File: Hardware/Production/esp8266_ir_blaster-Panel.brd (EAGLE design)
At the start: 97.3 x 103.8 mm, 384 parts, among them Q1 600mA/40V, Q2 600mA/40V, Q3 600mA/40V, Q4 600mA/40V, Q5 600mA/40V, Q6 600mA/40V, Q7 600mA/40V, Q8 600mA/40V, Q9 600mA/40V, U1 ESP-12S, U10 38kHz, U11 ESP-12S, U12 38kHz, U13 ESP-12S, U14 38kHz, U15 ESP-12S, U16 38kHz, U17 ESP-12S, U18 38kHz, U2 38kHz, U3 ESP-12S, U4 38kHz, U5 ESP-12S, U6 38kHz, U7 ESP-12S, U8 38kHz, U9 ESP-12S

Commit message: Revising LED color. Adding production panel.
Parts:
- D11, D14, D17, D2, D20, D23, D26, D5, D8: value BLUE -> GREEN
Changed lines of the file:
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@@
 <?xml version="1.0" encoding="utf-8"?>
 <!DOCTYPE eagle SYSTEM "eagle.dtd">
-<eagle version="9.0.1">
+<eagle version="9.1.1">
 <drawing>
 <settings>
@@
 <param name="checkStop" value="0"/>
 <param name="checkValues" value="0"/>
+<param name="checkNames" value="1"/>
+<param name="checkWireStubs" value="1"/>
+<param name="checkPolygonWidth" value="0"/>
 <param name="useDiameter" value="13"/>
 <param name="maxErrors" value="50"/>
@@
 <attribute name="PROD_ID" value="RES-07856" x="14.351" y="15.875" size="1.778" layer="27" font="vector" ratio="15" rot="R90" display="off"/>
 </element>
-<element name="D2" library="SparkFun-LED" package="LED-0603" value="BLUE" x="12.7" y="15.875" rot="R90">
-<attribute name="PROD_ID" value="DIO-08575" x="12.7" y="15.875" size="1.778" layer="27" font="vector" ratio="15" rot="R90" display="off"/>
+<element name="D2" library="SparkFun-LED" package="LED-0603" value="GREEN" x="12.7" y="15.875" rot="R90">
+<attribute name="PROD_ID" value="DIO-00821" x="12.7" y="15.875" size="1.778" layer="27" font="vector" ratio="15" rot="R90" display="off"/>
 </element>
 <element name="Q1" library="SparkFun-DiscreteSemi" package="SOT23-3" value="600mA/40V" x="13.97" y="5.08" rot="R90">
@@
 <attribute name="PROD_ID" value="RES-07856" x="40.259" y="15.875" size="1.778" layer="27" font="vector" ratio="15" rot="R90" display="off"/>
 </element>
-<element name="D5" library="SparkFun-LED" package="LED-0603" value="BLUE" x="38.608" y="15.875" rot="R90">
-<attribute name="PROD_ID" value="DIO-08575" x="38.608" y="15.875" size="1.778" layer="27" font="vector" ratio="15" rot="R90" display="off"/>
+<element name="D5" library="SparkFun-LED" package="LED-0603" value="GREEN" x="38.608" y="15.875" rot="R90">
+<attribute name="PROD_ID" value="DIO-00821" x="38.608" y="15.875" size="1.778" layer="27" font="vector" ratio="15" rot="R90" display="off"/>
 </element>
 <element name="Q2" library="SparkFun-DiscreteSemi" package="SOT23-3" value="600mA/40V" x="39.878" y="5.08" rot="R90">
@@
 <attribute name="PROD_ID" value="RES-07856" x="66.167" y="15.875" size="1.778" layer="27" font="vector" ratio="15" rot="R90" display="off"/>
 </element>
-<element name="D8" library="SparkFun-LED" package="LED-0603" value="BLUE" x="64.516" y="15.875" rot="R90">
-<attribute name="PROD_ID" value="DIO-08575" x="64.516" y="15.875" size="1.778" layer="27" font="vector" ratio="15" rot="R90" display="off"/>
+<element name="D8" library="SparkFun-LED" package="LED-0603" value="GREEN" x="64.516" y="15.875" rot="R90">
+<attribute name="PROD_ID" value="DIO-00821" x="64.516" y="15.875" size="1.778" layer="27" font="vector" ratio="15" rot="R90" display="off"/>
 </element>
 <element name="Q3" library="SparkFun-DiscreteSemi" package="SOT23-3" value="600mA/40V" x="65.786" y="5.08" rot="R90">
@@
 <attribute name="PROD_ID" value="RES-07856" x="14.351" y="43.942" size="1.778" layer="27" font="vector" ratio="15" rot="R90" display="off"/>
 </element>
-<element name="D11" library="SparkFun-LED" package="LED-0603" value="BLUE" x="12.7" y="43.942" rot="R90">
-<attribute name="PROD_ID" value="DIO-08575" x="12.7" y="43.942" size="1.778" layer="27" font="vector" ratio="15" rot="R90" display="off"/>
+<element name="D11" library="SparkFun-LED" package="LED-0603" value="GREEN" x="12.7" y="43.942" rot="R90">
+<attribute name="PROD_ID" value="DIO-00821" x="12.7" y="43.942" size="1.778" layer="27" font="vector" ratio="15" rot="R90" display="off"/>
 </element>
 <element name="Q4" library="SparkFun-DiscreteSemi" package="SOT23-3" value="600mA/40V" x="13.97" y="33.147" rot="R90">
@@
 <attribute name="PROD_ID" value="RES-07856" x="40.259" y="43.942" size="1.778" layer="27" font="vector" ratio="15" rot="R90" display="off"/>
 </element>
-<element name="D14" library="SparkFun-LED" package="LED-0603" value="BLUE" x="38.608" y="43.942" rot="R90">
-<attribute name="PROD_ID" value="DIO-08575" x="38.608" y="43.942" size="1.778" layer="27" font="vector" ratio="15" rot="R90" display="off"/>
+<element name="D14" library="SparkFun-LED" package="LED-0603" value="GREEN" x="38.608" y="43.942" rot="R90">
+<attribute name="PROD_ID" value="DIO-00821" x="38.608" y="43.942" size="1.778" layer="27" font="vector" ratio="15" rot="R90" display="off"/>
 </element>
 <element name="Q5" library="SparkFun-DiscreteSemi" package="SOT23-3" value="600mA/40V" x="39.878" y="33.147" rot="R90">
@@
 <attribute name="PROD_ID" value="RES-07856" x="66.167" y="43.942" size="1.778" layer="27" font="vector" ratio="15" rot="R90" display="off"/>
 </element>
-<element name="D17" library="SparkFun-LED" package="LED-0603" value="BLUE" x="64.516" y="43.942" rot="R90">
-<attribute name="PROD_ID" value="DIO-08575" x="64.516" y="43.942" size="1.778" layer="27" font="vector" ratio="15" rot="R90" display="off"/>
+<element name="D17" library="SparkFun-LED" package="LED-0603" value="GREEN" x="64.516" y="43.942" rot="R90">
+<attribute name="PROD_ID" value="DIO-00821" x="64.516" y="43.942" size="1.778" layer="27" font="vector" ratio="15" rot="R90" display="off"/>
 </element>
 <element name="Q6" library="SparkFun-DiscreteSemi" package="SOT23-3" value="600mA/40V" x="65.786" y="33.147" rot="R90">
@@
 <attribute name="PROD_ID" value="RES-07856" x="14.351" y="72.009" size="1.778" layer="27" font="vector" ratio="15" rot="R90" display="off"/>
 </element>
-<element name="D20" library="SparkFun-LED" package="LED-0603" value="BLUE" x="12.7" y="72.009" rot="R90">
-<attribute name="PROD_ID" value="DIO-08575" x="12.7" y="72.009" size="1.778" layer="27" font="vector" ratio="15" rot="R90" display="off"/>
+<element name="D20" library="SparkFun-LED" package="LED-0603" value="GREEN" x="12.7" y="72.009" rot="R90">
+<attribute name="PROD_ID" value="DIO-00821" x="12.7" y="72.009" size="1.778" layer="27" font="vector" ratio="15" rot="R90" display="off"/>
 </element>
 <element name="Q7" library="SparkFun-DiscreteSemi" package="SOT23-3" value="600mA/40V" x="13.97" y="61.214" rot="R90">
@@
 <attribute name="PROD_ID" value="RES-07856" x="40.259" y="72.009" size="1.778" layer="27" font="vector" ratio="15" rot="R90" display="off"/>
 </element>
-<element name="D23" library="SparkFun-LED" package="LED-0603" value="BLUE" x="38.608" y="72.009" rot="R90">
-<attribute name="PROD_ID" value="DIO-08575" x="38.608" y="72.009" size="1.778" layer="27" font="vector" ratio="15" rot="R90" display="off"/>
+<element name="D23" library="SparkFun-LED" package="LED-0603" value="GREEN" x="38.608" y="72.009" rot="R90">
+<attribute name="PROD_ID" value="DIO-00821" x="38.608" y="72.009" size="1.778" layer="27" font="vector" ratio="15" rot="R90" display="off"/>
 </element>
 <element name="Q8" library="SparkFun-DiscreteSemi" package="SOT23-3" value="600mA/40V" x="39.878" y="61.214" rot="R90">
@@
 <attribute name="PROD_ID" value="RES-07856" x="66.167" y="72.009" size="1.778" layer="27" font="vector" ratio="15" rot="R90" display="off"/>
 </element>
-<element name="D26" library="SparkFun-LED" package="LED-0603" value="BLUE" x="64.516" y="72.009" rot="R90">
-<attribute name="PROD_ID" value="DIO-08575" x="64.516" y="72.009" size="1.778" layer="27" font="vector" ratio="15" rot="R90" display="off"/>
+<element name="D26" library="SparkFun-LED" package="LED-0603" value="GREEN" x="64.516" y="72.009" rot="R90">
+<attribute name="PROD_ID" value="DIO-00821" x="64.516" y="72.009" size="1.778" layer="27" font="vector" ratio="15" rot="R90" display="off"/>
 </element>
 <element name="Q9" library="SparkFun-DiscreteSemi" package="SOT23-3" value="600mA/40V" x="65.786" y="61.214" rot="R90">
@@
 </signal>
 </signals>
+<mfgpreviewcolors>
+<mfgpreviewcolor name="soldermaskcolor" color="0xC8008000"/>
+<mfgpreviewcolor name="silkscreencolor" color="0xFFFEFEFE"/>
+<mfgpreviewcolor name="backgroundcolor" color="0xFF282828"/>
+<mfgpreviewcolor name="coppercolor" color="0xFFFFBF00"/>
+<mfgpreviewcolor name="substratecolor" color="0xFF786E46"/>
+</mfgpreviewcolors>
 </board>
 </drawing>

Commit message: x02 hardware commit
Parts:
- added C10, C11, C13, C14, C15, C17, C18, C19, C21, C22, C23, C25, C26, C27, C29, C30, C31, C33, C34, C35: 1.0uF, SparkFun-Capacitors:0603
- added C12, C16, C20, C24, C28, C32, C36: 2.2uF, SparkFun-Capacitors:0603
- added H1, H10, H11, H12, H13, H14, H15, H16, H17, H18, H2, H3, H4, H5, H6, H7, H8, H9: STAND-OFF, SparkFun-Hardware:STAND-OFF
- added R64, R68, R70, R72: 1k, SparkFun-Resistors:0603
- added R65, R66, R67, R71: 10k, SparkFun-Resistors:0603
- added R69: 20, SparkFun-Resistors:0603
- added U$154, U$174: (no value), buzzard_labels:VIN6
- added U$155, U$168, U$175: (no value), buzzard_labels:GND5
- added U$156, U$176: (no value), buzzard_labels:512
- added U$157, U$167, U$177: (no value), buzzard_labels:3#3V4
- added U$158, U$178: (no value), buzzard_labels:SLP14
- added U$159, U$161, U$179: (no value), buzzard_labels:WIFI_IR_BLASTER11
- added U$160, U$180: (no value), buzzard_labels-02:UART0
- added U$162: (no value), buzzard_labels:013
- added U$163: (no value), buzzard_labels:RST14
- added U$164: (no value), buzzard_labels:DTR1
- added U$165: (no value), buzzard_labels:TX2
- added U$166: (no value), buzzard_labels:RX3
- added U$169: (no value), buzzard_labels:511
- added U$170: (no value), buzzard_labels:ADC10
- added U$171: (no value), buzzard_labels:129
- added U$172: (no value), buzzard_labels:148
- added U$173: (no value), buzzard_labels:27
- added U19, U22, U25: ESP-12S, esp8266_ir_blaster:ESP-12S
- added U20, U23, U26: 38kHz, esp8266_ir_blaster:TSOP382
- added U21, U24, U27: 3.3V, SparkFun-IC-Power:SOT23-5
- C4, C8: value 1.0uF -> 2.2uF
- J1, J11, J13, J15, J17, J9: device SparkFun-Connectors:1X06 -> SparkFun-Connectors:1X06_NO_SILK
- J10, J12, J14, J16, J18, J8: device SparkFun-Connectors:1X07 -> SparkFun-Connectors:1X08_NO_SILK
- J2, J4, J6: device SparkFun-Connectors:1X06 -> SparkFun-Connectors:1X08_NO_SILK
- J3, J5, J7: device SparkFun-Connectors:1X07 -> SparkFun-Connectors:1X06_NO_SILK
- R11, R18, R25, R27, R34, R39, R41, R55: value 1k -> 10k
- R12, R40, R54: value 68 -> 1k
- R13, R53: value 1k -> 20
- R14, R16, R22, R24, R28, R3, R30, R36, R38, R44, R52, R56: value 10k -> 1k
- R19, R26, R33, R47: value 68 -> 10k
- R21, R29, R37, R45: value 10k -> 20
- R6, R61: value 68 -> 20
- U$1: device buzzard_labels:GND11 -> buzzard_labels:512
- U$10: device buzzard_labels:RX3 -> buzzard_labels:129
- U$100: device buzzard_labels:RST14 -> buzzard_labels-02:UART0
- U$101, U$99: device buzzard_labels:013 -> buzzard_labels:WIFI_IR_BLASTER11
- U$102: device buzzard_labels:SLEEP15 -> buzzard_labels:013
- U$103: device buzzard_labels:GND11 -> buzzard_labels:RST14
- U$104: device buzzard_labels:3#3V12 -> buzzard_labels:DTR1
- U$105: device buzzard_labels:210 -> buzzard_labels:TX2
- U$106: device buzzard_labels:149 -> buzzard_labels:RX3
- U$107: device buzzard_labels:127 -> buzzard_labels:3#3V4
- U$108: device buzzard_labels:ADC6 -> buzzard_labels:GND5
- U$109: device buzzard_labels:58 -> buzzard_labels:511
- U$11: device buzzard_labels:TX4 -> buzzard_labels:148
- U$110: device buzzard_labels:GND1 -> buzzard_labels:ADC10
- U$111: device buzzard_labels:3#3V2 -> buzzard_labels:129
- U$112: device buzzard_labels:RX3 -> buzzard_labels:148
- U$113: device buzzard_labels:TX4 -> buzzard_labels:27
- U$114: device buzzard_labels:DTR5 -> buzzard_labels:VIN6
- U$115: device buzzard_labels:WIFI_IR_BLASTER11 -> buzzard_labels:GND5
- U$116: device buzzard_labels:013 -> buzzard_labels:512
- U$117: device buzzard_labels:RST14 -> buzzard_labels:3#3V4
- U$118: device buzzard_labels:013 -> buzzard_labels:SLP14
- U$119: device buzzard_labels:SLEEP15 -> buzzard_labels:WIFI_IR_BLASTER11
- U$12: device buzzard_labels:DTR5 -> buzzard_labels:27
- U$120: device buzzard_labels:GND11 -> buzzard_labels-02:UART0
- U$121: device buzzard_labels:3#3V12 -> buzzard_labels:WIFI_IR_BLASTER11
- U$122: device buzzard_labels:210 -> buzzard_labels:013
- U$123: device buzzard_labels:149 -> buzzard_labels:RST14
- U$124: device buzzard_labels:127 -> buzzard_labels:DTR1
- U$125: device buzzard_labels:ADC6 -> buzzard_labels:TX2
- U$126: device buzzard_labels:58 -> buzzard_labels:RX3
- U$127: device buzzard_labels:GND1 -> buzzard_labels:3#3V4
- U$128: device buzzard_labels:3#3V2 -> buzzard_labels:GND5
- U$129: device buzzard_labels:RX3 -> buzzard_labels:511
- U$130: device buzzard_labels:TX4 -> buzzard_labels:ADC10
- U$131: device buzzard_labels:DTR5 -> buzzard_labels:129
- U$132: device buzzard_labels:WIFI_IR_BLASTER11 -> buzzard_labels:148
- U$133, U$33: device buzzard_labels:013 -> buzzard_labels:27
- U$134: device buzzard_labels:RST14 -> buzzard_labels:VIN6
- U$135, U$48: device buzzard_labels:013 -> buzzard_labels:GND5
- U$136: device buzzard_labels:SLEEP15 -> buzzard_labels:512
- U$137: device buzzard_labels:GND11 -> buzzard_labels:3#3V4
- U$138: device buzzard_labels:3#3V12 -> buzzard_labels:SLP14
- U$139: device buzzard_labels:210 -> buzzard_labels:WIFI_IR_BLASTER11
- U$140: device buzzard_labels:149 -> buzzard_labels-02:UART0
- U$141, U$39: device buzzard_labels:127 -> buzzard_labels:WIFI_IR_BLASTER11
- U$142: device buzzard_labels:ADC6 -> buzzard_labels:013
- U$143: device buzzard_labels:58 -> buzzard_labels:RST14
- U$144: device buzzard_labels:GND1 -> buzzard_labels:DTR1
- U$145: device buzzard_labels:3#3V2 -> buzzard_labels:TX2
- U$147: device buzzard_labels:TX4 -> buzzard_labels:3#3V4
- U$148: device buzzard_labels:DTR5 -> buzzard_labels:GND5
- U$149: device buzzard_labels:WIFI_IR_BLASTER11 -> buzzard_labels:511
- U$150, U$50: device buzzard_labels:013 -> buzzard_labels:ADC10
- U$151: device buzzard_labels:RST14 -> buzzard_labels:129
- U$152: device buzzard_labels:013 -> buzzard_labels:148
- U$153: device buzzard_labels:SLEEP15 -> buzzard_labels:27
- U$17: device buzzard_labels:SLEEP15 -> buzzard_labels:RST14
- U$18: device buzzard_labels:GND11 -> buzzard_labels:DTR1
- U$19: device buzzard_labels:3#3V12 -> buzzard_labels:TX2
- U$2, U$87: device buzzard_labels:3#3V12 -> buzzard_labels:3#3V4
- U$20: device buzzard_labels:210 -> buzzard_labels:RX3
- U$21: device buzzard_labels:149 -> buzzard_labels:3#3V4
- U$22: device buzzard_labels:127 -> buzzard_labels:GND5
- U$23, U$74: device buzzard_labels:ADC6 -> buzzard_labels:VIN6
- U$24, U$75: device buzzard_labels:58 -> buzzard_labels:GND5
- U$25: device buzzard_labels:GND1 -> buzzard_labels:TX2
- U$26: device buzzard_labels:3#3V2 -> buzzard_labels:RX3
- U$27: device buzzard_labels:RX3 -> buzzard_labels:3#3V4
- U$28: device buzzard_labels:TX4 -> buzzard_labels:GND5
- U$29: device buzzard_labels:DTR5 -> buzzard_labels:511
- U$3: device buzzard_labels:210 -> buzzard_labels:SLP14
- U$30: device buzzard_labels:WIFI_IR_BLASTER11 -> buzzard_labels:ADC10
- U$31: device buzzard_labels:013 -> buzzard_labels:129
- U$32: device buzzard_labels:RST14 -> buzzard_labels:148
- U$34: device buzzard_labels:SLEEP15 -> buzzard_labels:VIN6
- U$35: device buzzard_labels:GND11 -> buzzard_labels:GND5
- U$36: device buzzard_labels:3#3V12 -> buzzard_labels:512
- U$37: device buzzard_labels:210 -> buzzard_labels:3#3V4
- U$38: device buzzard_labels:149 -> buzzard_labels:SLP14
- U$4: device buzzard_labels:149 -> buzzard_labels:WIFI_IR_BLASTER11
- U$40: device buzzard_labels:ADC6 -> buzzard_labels-02:UART0
- U$41, U$7: device buzzard_labels:58 -> buzzard_labels:WIFI_IR_BLASTER11
- U$42: device buzzard_labels:GND1 -> buzzard_labels:013
- U$43: device buzzard_labels:3#3V2 -> buzzard_labels:RST14
- U$44: device buzzard_labels:RX3 -> buzzard_labels:DTR1
- U$45: device buzzard_labels:TX4 -> buzzard_labels:TX2
- U$46: device buzzard_labels:DTR5 -> buzzard_labels:RX3
- U$47: device buzzard_labels:WIFI_IR_BLASTER11 -> buzzard_labels:3#3V4
- U$49: device buzzard_labels:RST14 -> buzzard_labels:511
- U$5: device buzzard_labels:127 -> buzzard_labels-02:UART0
- U$51: device buzzard_labels:SLEEP15 -> buzzard_labels:129
- U$52: device buzzard_labels:GND11 -> buzzard_labels:148
- U$53: device buzzard_labels:3#3V12 -> buzzard_labels:27
- U$54: device buzzard_labels:210 -> buzzard_labels:VIN6
- U$55: device buzzard_labels:149 -> buzzard_labels:GND5
- U$56: device buzzard_labels:127 -> buzzard_labels:512
- U$57: device buzzard_labels:ADC6 -> buzzard_labels:3#3V4
- U$58: device buzzard_labels:58 -> buzzard_labels:SLP14
- U$59: device buzzard_labels:GND1 -> buzzard_labels:WIFI_IR_BLASTER11
- U$6: device buzzard_labels:ADC6 -> buzzard_labels:DTR1
- U$60: device buzzard_labels:3#3V2 -> buzzard_labels-02:UART0
- U$61: device buzzard_labels:RX3 -> buzzard_labels:WIFI_IR_BLASTER11
- U$62: device buzzard_labels:TX4 -> buzzard_labels:013
- U$63: device buzzard_labels:DTR5 -> buzzard_labels:RST14
- U$64: device buzzard_labels:WIFI_IR_BLASTER11 -> buzzard_labels:DTR1
- U$65: device buzzard_labels:013 -> buzzard_labels:TX2
- U$66: device buzzard_labels:RST14 -> buzzard_labels:RX3
- U$67: device buzzard_labels:013 -> buzzard_labels:3#3V4
- U$68: device buzzard_labels:SLEEP15 -> buzzard_labels:GND5
- U$69: device buzzard_labels:GND11 -> buzzard_labels:511
- U$70: device buzzard_labels:3#3V12 -> buzzard_labels:ADC10
- U$71: device buzzard_labels:210 -> buzzard_labels:129
- U$72: device buzzard_labels:149 -> buzzard_labels:148
- U$73: device buzzard_labels:127 -> buzzard_labels:27
- U$76: device buzzard_labels:GND1 -> buzzard_labels:512
- U$77: device buzzard_labels:3#3V2 -> buzzard_labels:3#3V4
- U$78: device buzzard_labels:RX3 -> buzzard_labels:SLP14
- U$79: device buzzard_labels:TX4 -> buzzard_labels:WIFI_IR_BLASTER11
- U$8: device buzzard_labels:GND1 -> buzzard_labels:511
- U$80: device buzzard_labels:DTR5 -> buzzard_labels-02:UART0
- U$84: device buzzard_labels:013 -> buzzard_labels:DTR1
- U$85: device buzzard_labels:SLEEP15 -> buzzard_labels:TX2
- U$86: device buzzard_labels:GND11 -> buzzard_labels:RX3
- U$88: device buzzard_labels:210 -> buzzard_labels:GND5
- U$89: device buzzard_labels:149 -> buzzard_labels:511
- U$9: device buzzard_labels:3#3V2 -> buzzard_labels:ADC10
- U$90: device buzzard_labels:127 -> buzzard_labels:ADC10
- U$91: device buzzard_labels:ADC6 -> buzzard_labels:129
- U$92: device buzzard_labels:58 -> buzzard_labels:148
- U$93: device buzzard_labels:GND1 -> buzzard_labels:27
- U$94: device buzzard_labels:3#3V2 -> buzzard_labels:VIN6
- U$95: device buzzard_labels:RX3 -> buzzard_labels:GND5
- U$96: device buzzard_labels:TX4 -> buzzard_labels:512
- U$97: device buzzard_labels:DTR5 -> buzzard_labels:3#3V4
- U$98: device buzzard_labels:WIFI_IR_BLASTER11 -> buzzard_labels:SLP14
- U10, U16, U4: value 38kHz -> ESP-12S; device esp8266_ir_blaster:TSOP382 -> esp8266_ir_blaster:ESP-12S
- U11, U17, U5: value ESP-12S -> 38kHz; device esp8266_ir_blaster:ESP-12S -> esp8266_ir_blaster:TSOP382
- U12, U18, U6: value 38kHz -> 3.3V; device esp8266_ir_blaster:TSOP382 -> SparkFun-IC-Power:SOT23-5
- U15, U3, U9: value ESP-12S -> 3.3V; device esp8266_ir_blaster:ESP-12S -> SparkFun-IC-Power:SOT23-5
- moved J6 82.8 mm to (75.9, 6.35), turned to 90 degrees
- moved U$115 77.2 mm to (70.9, 39.5)
- moved U$59 76.1 mm to (73.4, 2.46), flipped to the bottom
- moved U$114 74.7 mm to (71.2, 42.0)
- moved U$140 74.4 mm to (1.27, 87.1), flipped to the bottom, turned to 90 degrees
- moved U$113 73.7 mm to (73.0, 47.1)
- moved U$112 71.4 mm to (72.4, 52.2)
- moved U$111 71.1 mm to (72.1, 49.7)
- moved U$117 68.7 mm to (70.6, 44.6)
- moved U$110 68.6 mm to (70.7, 54.7)
- moved U$119 67.9 mm to (73.4, 35.6), flipped to the bottom
- moved U$118 66.7 mm to (77.0, 61.3), flipped to the bottom
- moved R44 66.1 mm to (69.0, 47.1), turned to 0 degrees
- moved R22 65.9 mm to (66.7, 11.4), turned to 90 degrees
- moved C7 64.1 mm to (38.7, 11.4)
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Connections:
- removed net N$13 (its old number): D11.C, R25.2
- removed net N$17 (its old number): D14.C, R32.2
- removed net N$2 (its old number): D2.C, R5.2
- removed net N$21 (its old number): D17.C, R39.2
- removed net N$25 (its old number): D20.C, R46.2
- removed net N$29 (its old number): D23.C, R53.2
- removed net N$33 (its old number): D26.C, R60.2
- removed net N$9 (its old number): D8.C, R18.2
- new net N$10: D7.A, R21.1
- new net N$14: D10.A, R29.1
- new net N$18: D13.A, R37.1
- new net N$22: D16.A, R45.1
- new net N$26: D19.A, R53.1
- new net N$3: D4.A, R13.1
- new net N$30: D22.A, R61.1
- new net N$34: D25.A, R69.1
- new net VIN: C3.1, J2.2, U3.1, U3.3
- new net VIN1: C7.1, J4.2, U6.1, U6.3
- new net VIN2: C11.1, J6.2, U9.1, U9.3
- new net VIN3: C15.1, J8.2, U12.1, U12.3
- new net VIN4: C19.1, J10.2, U15.1, U15.3
- new net VIN5: C23.1, J12.2, U18.1, U18.3
- new net VIN6: C27.1, J14.2, U21.1, U21.3
- new net VIN7: C31.1, J16.2, U24.1, U24.3
- new net VIN8: C35.1, J18.2, U27.1, U27.3
- net 3.3V: now also C4.1, J2.3, R5.2, U3.5; no longer D2.A, J8.2
- net 3.3V1: now also C5.1, C8.1, J3.4, J4.3, R10.1, R13.2, R15.1, R9.2, U4.8, U5.3, U6.5; no longer C2.1, D5.A, J2.4, J3.2, R14.1, R3.2, R9.1, U3.8, U4.3
- net 3.3V2: now also C12.1, C9.1, J5.4, J6.3, R17.2, R18.1, R20.2, R21.2, R23.1, U7.8, U8.3, U9.5; no longer C3.1, D8.A, J4.4, J5.2, R15.2, R16.1, R19.2, R21.1, U5.8, U6.3
- net 3.3V3: now also C13.1, C16.1, J7.4, J8.3, R25.2, R26.1, R28.2, R29.2, R31.1, U10.8, U11.3, U12.5; no longer C4.1, D11.A, J6.4, J7.2, R22.2, R23.1, R26.2, R28.1, U7.8, U8.3
- net 3.3V4: now also C17.1, C20.1, J10.3, R34.1, R36.2, R37.2, R39.1, U13.8, U14.3, U15.5; no longer C5.1, D14.A, J10.2, R29.2, R30.1, R35.1, U10.3, U9.8
- net 3.3V5: now also C21.1, C24.1, J12.3, R41.2, R44.2, R45.2, R47.1, U16.8, U17.3, U18.5; no longer C6.1, D17.A, J12.2, R36.2, R37.1, R40.2, U11.8, U12.3
- net 3.3V6: now also C25.1, C28.1, J14.3, R49.2, R50.1, R52.2, R53.2, R55.1, U19.8, U20.3, U21.5; no longer C7.1, D20.A, J14.2, R43.2, R44.1, R47.2, R49.1, U13.8, U14.3
- net 3.3V7: now also C29.1, C32.1, J16.3, R57.2, R58.1, R60.2, R61.2, R63.1, U22.8, U23.3, U24.5; no longer C8.1, D23.A, J16.2, R50.2, R51.1, R54.2, R56.1, U15.8, U16.3
- net 3.3V8: now also C33.1, C36.1, J18.3, R65.2, R66.1, R68.2, R69.2, R71.1, U25.8, U26.3, U27.5; no longer C9.1, D26.A, J18.2, R57.2, R58.1, R61.2, R63.1, U17.8, U18.3
- net ADC: now also J2.7; no longer J8.6
- net ADC1: now also J4.7, U4.2; no longer J3.6, U3.2
- net ADC2: now also J6.7, U7.2; no longer J5.6, U5.2
- net ADC3: now also J8.7, U10.2; no longer J7.6, U7.2
- net ADC4: now also J10.7, U13.2; no longer J10.6, U9.2
- net ADC5: now also J12.7, U16.2; no longer J12.6, U11.2
- net ADC6: now also J14.7, U19.2; no longer J14.6, U13.2
- net ADC7: now also J16.7, U22.2; no longer J16.6, U15.2
- net ADC8: now also J18.7, U25.2; no longer J18.6, U17.2
- net CHIP_EN1: now also R10.2, U4.3; no longer R9.2, U3.3
- net CHIP_EN2: now also R18.2, U7.3; no longer R16.2, U5.3
- net CHIP_EN3: now also R26.2, U10.3; no longer R23.2, U7.3
- net CHIP_EN4: now also R34.2, U13.3; no longer R30.2, U9.3
- net CHIP_EN5: now also R42.2, U16.3; no longer R37.2, U11.3
- net CHIP_EN6: now also R50.2, U19.3; no longer R44.2, U13.3
- net CHIP_EN7: now also R58.2, U22.3; no longer R51.2, U15.3
- net CHIP_EN8: now also R66.2, U25.3; no longer R58.2, U17.3
- net DTR: now also C2.2
- net DTR1: now also C6.2, J3.1; no longer J2.1
- net DTR2: now also C10.2, J5.1; no longer J4.1
- net DTR3: now also C14.2, J7.1; no longer J6.1
- net DTR4: now also C18.2
- net DTR5: now also C22.2
- net DTR6: now also C26.2
- net DTR7: now also C30.2
- net DTR8: now also C34.2
- net GND: now also C3.2, C4.2, J2.1, R3.1, U3.2; no longer J8.1
- net GND1: now also C5.2, C7.2, C8.2, J3.6, J4.1, R11.2, R16.1, U4.9, U5.2, U6.2; no longer C2.2, J2.6, J3.1, R10.2, U3.9, U4.2
- net GND2: now also C11.2, C12.2, C9.2, J5.6, J6.1, R19.2, R24.1, U7.9, U8.2, U9.2; no longer C3.2, J4.6, J5.1, R17.2, U5.9, U6.2
- net GND3: now also C13.2, C15.2, C16.2, J7.6, J8.1, R27.2, R32.1, U10.9, U11.2, U12.2; no longer C4.2, J6.6, J7.1, R24.2, U7.9, U8.2
- net GND4: now also C17.2, C19.2, C20.2, R35.2, R40.1, U13.9, U14.2, U15.2; no longer C5.2, R31.2, U10.2, U9.9
- net GND5: now also C21.2, C23.2, C24.2, R43.2, R48.1, U16.9, U17.2, U18.2; no longer C6.2, R38.2, U11.9, U12.2
- net GND6: now also C25.2, C27.2, C28.2, R51.2, R56.1, U19.9, U20.2, U21.2; no longer C7.2, R45.2, U13.9, U14.2
- net GND7: now also C29.2, C31.2, C32.2, R59.2, R64.1, U22.9, U23.2, U24.2; no longer C8.2, R52.2, U15.9, U16.2
- net GND8: now also C33.2, C35.2, C36.2, R67.2, R72.1, U25.9, U26.2, U27.2; no longer C9.2, R59.2, U17.9, U18.2
- net IO1: now also R11.1, U4.10; no longer R10.1, U3.10
- net IO10: now also R19.1, U7.10; no longer R17.1, U5.10
- net IO11: now also J6.4, R17.1, U7.11; no longer J5.3, R15.1, U5.11
- net IO12: now also J2.5; no longer J8.5
- net IO13: now also R20.1, U7.12; no longer R18.1, U5.12
- net IO14: now also J2.6; no longer J8.4
- net IO17: now also J6.6, U7.5; no longer J5.4, U5.5
- net IO18: now also U7.4; no longer U5.4
- net IO19: now also J6.5, U7.6; no longer J5.5, U5.6
- net IO2: now also J2.4; no longer J8.3
- net IO20: now also D8.A, J6.8, U7.14; no longer J5.7, U5.14
- net IO21: now also R27.1, U10.10; no longer R24.1, U7.10
- net IO22: now also J8.4, R25.1, U10.11; no longer J7.3, R22.1, U7.11
- net IO23: now also R28.1, U10.12; no longer R25.1, U7.12
- net IO24: now also J8.6, U10.5; no longer J7.4, U7.5
- net IO25: now also U10.4; no longer U7.4
- net IO26: now also J8.5, U10.6; no longer J7.5, U7.6
- net IO27: now also D11.A, J8.8, U10.14; no longer J7.7, U7.14
- net IO28: now also R35.1, U13.10; no longer R31.1, U9.10
- net IO29: now also J10.4, R33.1, U13.11; no longer J10.3, R29.1, U9.11
- net IO3: now also J4.4, R9.1, U4.11; no longer J3.3, R3.1, U3.11
- net IO30: now also R36.1, U13.12; no longer R32.1, U9.12
- net IO31: now also J10.6, U13.5; no longer J10.4, U9.5
- net IO32: now also U13.4; no longer U9.4
- net IO33: now also U13.6; no longer U9.6
- net IO34: now also D14.A, J10.8, U13.14; no longer J10.7, U9.14
- net IO35: now also R43.1, U16.10; no longer R38.1, U11.10
- net IO36: now also J12.4, R41.1, U16.11; no longer J12.3, R36.1, U11.11
- net IO37: now also R44.1, U16.12; no longer R39.1, U11.12
- net IO38: now also J12.6, U16.5; no longer J12.4, U11.5
- net IO39: now also U16.4; no longer U11.4
- net IO4: now also R12.1, U4.12; no longer R11.1, U3.12
- net IO40: now also U16.6; no longer U11.6
- net IO41: now also D17.A, J12.8, U16.14; no longer J12.7, U11.14
- net IO42: now also R51.1, U19.10; no longer R45.1, U13.10
- net IO43: now also J14.4, R49.1, U19.11; no longer J14.3, R43.1, U13.11
- net IO44: now also R52.1, U19.12; no longer R46.1, U13.12
- net IO45: now also J14.6, U19.5; no longer J14.4, U13.5
- net IO46: now also U19.4; no longer U13.4
- net IO47: now also U19.6; no longer U13.6
- net IO48: now also D20.A, J14.8, U19.14; no longer J14.7, U13.14
- net IO49: now also R59.1, U22.10; no longer R52.1, U15.10
- net IO5: now also D2.A, J2.8; no longer J8.7
- net IO50: now also J16.4, R57.1, U22.11; no longer J16.3, R50.1, U15.11
- net IO51: now also R60.1, U22.12; no longer R53.1, U15.12
- net IO52: now also J16.6, U22.5; no longer J16.4, U15.5
- net IO53: now also U22.4; no longer U15.4
- net IO54: now also U22.6; no longer U15.6
- net IO55: now also D23.A, J16.8, U22.14; no longer J16.7, U15.14
- net IO56: now also R67.1, U25.10; no longer R59.1, U17.10
- net IO57: now also J18.4, R65.1, U25.11; no longer J18.3, R57.1, U17.11
- net IO58: now also R68.1, U25.12; no longer R60.1, U17.12
- net IO59: now also J18.6, U25.5; no longer J18.4, U17.5
- net IO6: now also J4.6, U4.5; no longer J3.4, U3.5
- net IO60: now also U25.4; no longer U17.4
- net IO61: now also U25.6; no longer U17.6
- net IO62: now also D26.A, J18.8, U25.14; no longer J18.7, U17.14
- net IO7: now also U4.4; no longer U3.4
- net IO8: now also J4.5, U4.6; no longer J3.5, U3.6
- net IO9: now also D5.A, J4.8, U4.14; no longer J3.7, U3.14
- net IR_IN1: now also U4.7, U5.1; no longer U3.7, U4.1
- net IR_IN2: now also U7.7, U8.1; no longer U5.7, U6.1
- net IR_IN3: now also U10.7, U11.1; no longer U7.7, U8.1
- net IR_IN4: now also U13.7, U14.1; no longer U10.1, U9.7
- net IR_IN5: now also U16.7, U17.1; no longer U11.7, U12.1
- net IR_IN6: now also U19.7, U20.1; no longer U13.7, U14.1
- net IR_IN7: now also U22.7, U23.1; no longer U15.7, U16.1
- net IR_IN8: now also U25.7, U26.1; no longer U17.7, U18.1
- net IR_OUT1: now also R14.2, U4.13; no longer R13.2, U3.13
- net IR_OUT2: now also R22.2, U7.13; no longer R20.2, U5.13
- net IR_OUT3: now also R30.2, U10.13; no longer R27.2, U7.13
- net IR_OUT4: now also R38.2, U13.13; no longer R34.2, U9.13
- net IR_OUT5: now also R46.2, U16.13; no longer R41.2, U11.13
- net IR_OUT6: now also R54.2, U19.13; no longer R48.2, U13.13
- net IR_OUT7: now also R62.2, U22.13; no longer R55.2, U15.13
- net IR_OUT8: now also R70.2, U25.13; no longer R62.2, U17.13
- net N$1: now also D2.C, R3.2; no longer D5.C, R11.2
- net N$11: now also Q3.1, R22.1; no longer D7.A, R19.1
- net N$12: now also D8.C, R24.2; no longer Q3.1, R20.1
- net N$15: now also Q4.1, R30.1; no longer D10.A, R26.1
- net N$16: now also D11.C, R32.2; no longer Q4.1, R27.1
- net N$19: now also Q5.1, R38.1; no longer D13.A, R33.1
- net N$20: now also D14.C, R40.2; no longer Q5.1, R34.1
- net N$23: now also Q6.1, R46.1; no longer D16.A, R40.1
- net N$24: now also D17.C, R48.2; no longer Q6.1, R41.1
- net N$27: now also Q7.1, R54.1; no longer D19.A, R47.1
- net N$28: now also D20.C, R56.2; no longer Q7.1, R48.1
- net N$31: now also Q8.1, R62.1; no longer D22.A, R54.1
- net N$32: now also D23.C, R64.2; no longer Q8.1, R55.1
- net N$35: now also Q9.1, R70.1; no longer D25.A, R61.1
- net N$36: now also D26.C, R72.2; no longer Q9.1, R62.1
- net N$4: now also Q2.1, R14.1; no longer D4.A, R12.1
- net N$8: now also D5.C, R16.2; no longer Q2.1, R13.1
- net RESET: now also C2.1
- net RESET1: now also C6.1, R15.2, U4.1; no longer R14.2, U3.1
- net RESET2: now also C10.1, R23.2, U7.1; no longer R21.2, U5.1
- net RESET3: now also C14.1, R31.2, U10.1; no longer R28.2, U7.1
- net RESET4: now also C18.1, R39.2, U13.1; no longer R35.2, U9.1
- net RESET5: now also C22.1, R47.2, U16.1; no longer R42.2, U11.1
- net RESET6: now also C26.1, R55.2, U19.1; no longer R49.2, U13.1
- net RESET7: now also C30.1, R63.2, U22.1; no longer R56.2, U15.1
- net RESET8: now also C34.1, R71.2, U25.1; no longer R63.2, U17.1
- net RXI1: now also J3.3, U4.15; no longer J2.3, U3.15
- net RXI2: now also J5.3, U7.15; no longer J4.3, U5.15
- net RXI3: now also J7.3, U10.15; no longer J6.3, U7.15
- net RXI4: now also U13.15; no longer U9.15
- net RXI5: now also U16.15; no longer U11.15
- net RXI6: now also U19.15; no longer U13.15
- net RXI7: now also U22.15; no longer U15.15
- net RXI8: now also U25.15; no longer U17.15
- net TXO1: now also J3.2, U4.16; no longer J2.2, U3.16
- net TXO2: now also J5.2, U7.16; no longer J4.2, U5.16
- net TXO3: now also J7.2, U10.16; no longer J6.2, U7.16
- net TXO4: now also U13.16; no longer U9.16
- net TXO5: now also U16.16; no longer U11.16
- net TXO6: now also U19.16; no longer U13.16
- net TXO7: now also U22.16; no longer U15.16
- net TXO8: now also U25.16; no longer U17.16
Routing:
- net VIN2: track 0.00 -> 17.9 mm, vias 0 -> 1
- net VIN8: track 0.00 -> 17.9 mm, vias 0 -> 1
- net VIN6: track 0.00 -> 17.9 mm, vias 0 -> 1
- net VIN: track 0.00 -> 17.9 mm, vias 0 -> 1
- net VIN5: track 0.00 -> 17.9 mm, vias 0 -> 1
- net VIN1: track 0.00 -> 17.9 mm, vias 0 -> 1
- net VIN7: track 0.00 -> 17.9 mm, vias 0 -> 1
- net VIN3: track 0.00 -> 17.9 mm, vias 0 -> 1
- net VIN4: track 0.00 -> 17.9 mm, vias 0 -> 1
- net 3.3V3: track 52.9 -> 67.1 mm, vias 4 -> 3
- net 3.3V4: track 52.9 -> 67.1 mm, vias 4 -> 3
- net 3.3V1: track 52.9 -> 67.1 mm, vias 4 -> 3
- net 3.3V: track 52.9 -> 67.1 mm, vias 4 -> 3
- net 3.3V7: track 52.9 -> 67.1 mm, vias 4 -> 3
- net 3.3V5: track 52.9 -> 67.1 mm, vias 4 -> 3
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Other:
- board size 97.3 x 103.8 mm -> 97.3 x 119 mm
- board text added: "x02"
- board text removed: "x01"

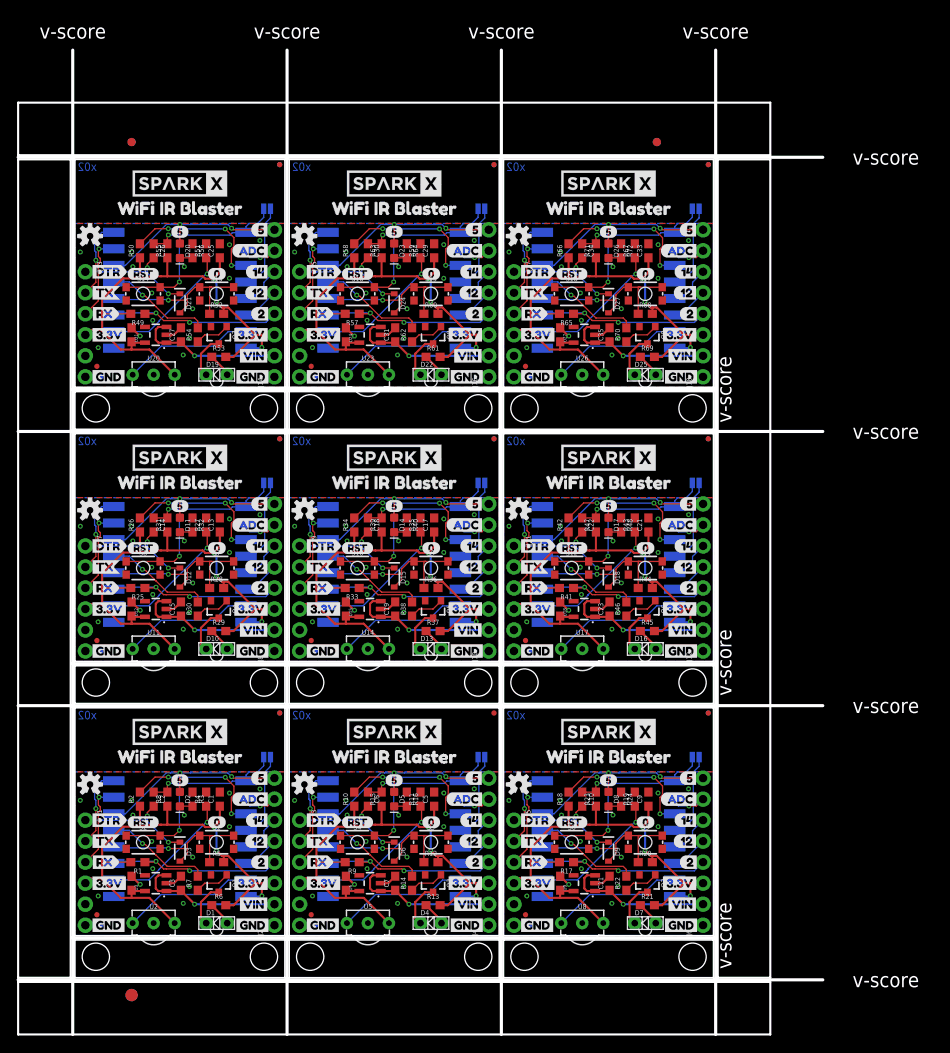
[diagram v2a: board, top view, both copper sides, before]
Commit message: Increasing drill size for IR receiver holes.
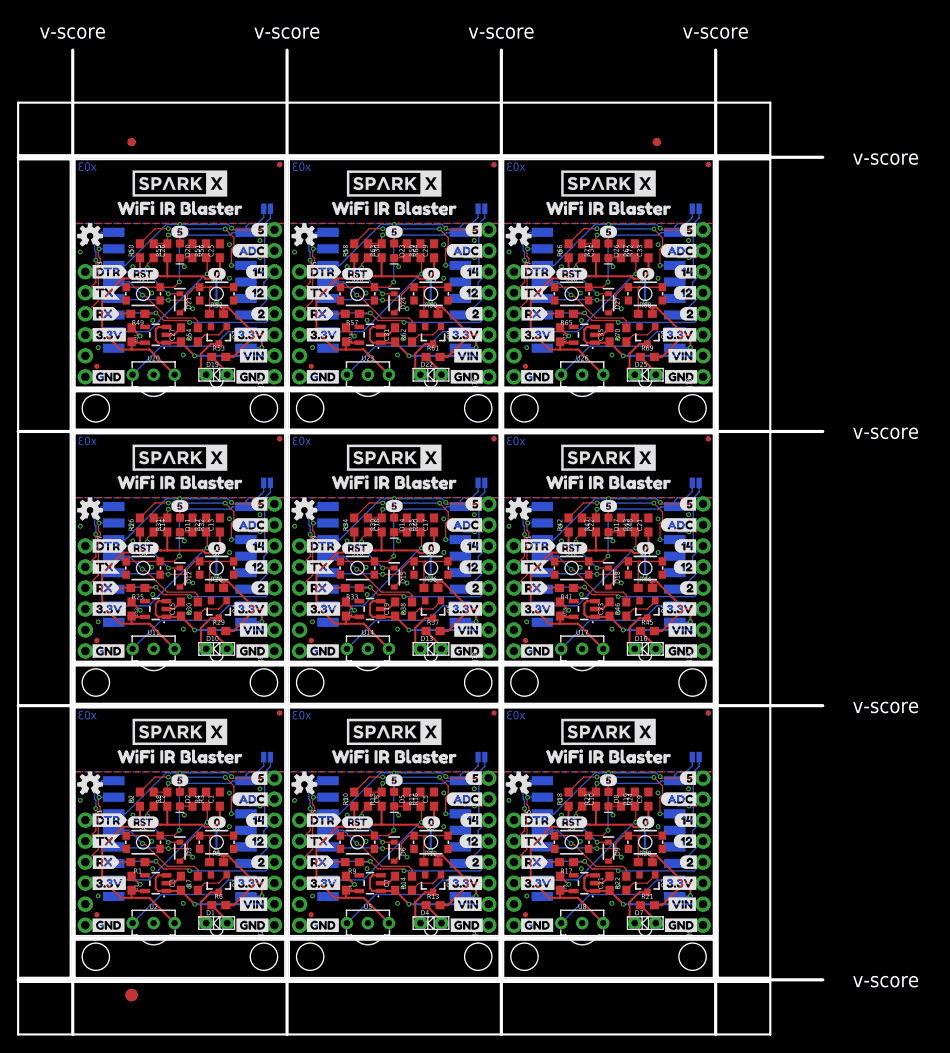
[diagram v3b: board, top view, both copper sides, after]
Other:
- board text added: "x03"
- board text removed: "x02"
